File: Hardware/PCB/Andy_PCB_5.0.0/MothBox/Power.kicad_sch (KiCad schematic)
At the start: 23 parts, among them J1 Screw_Terminal_01x02, J2 TYPE-C-31-M-17, Q1 IRF9540N, Q2 TJ10S04M3L,LXHQ, Q3 BC817, U1 XL4015, U2 9V-36V to 12V 5A 60W

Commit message: Andy Added Bolts an consolidated projects
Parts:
- added TPname: TestPoint, TestPoint:TestPoint_THTPad_1.0x1.0mm_Drill0.5mm, symbol Connector:TestPoint
- added U7: ~, symbol attractor:camera2
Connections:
- net at E1.1 (K), F1.1, Q1.3 (S): now also TPname.1
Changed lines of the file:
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@@
+	)
+	(symbol
+		(lib_id "attractor:camera2")
+		(at 110.49 68.58 0)
+		(unit 1)
+		(exclude_from_sim no)
+		(in_bom yes)
+		(on_board yes)
+		(dnp no)
+		(fields_autoplaced yes)
+		(property "Reference" "U7"
+			(at 121.92 67.9449 0)
+			(effects
+				(font
+					(size 1.27 1.27)
+				)
+				(justify left)
+			)
+		)
+		(property "Value" "~"
+			(at 121.92 69.85 0)
+			(effects
+				(font
+					(size 1.27 1.27)
+				)
+				(justify left)
+			)
+		)
+		(property "Footprint" ""
+			(at 110.49 68.58 0)
+			(effects
+				(font
+					(size 1.27 1.27)
+				)
+				(hide yes)
+			)
+		)
+		(property "Datasheet" ""
+			(at 110.49 68.58 0)
+			(effects
+				(font
+					(size 1.27 1.27)
+				)
+				(hide yes)
+			)
+		)
+		(property "Description" ""
+			(at 110.49 68.58 0)
+			(effects
+				(font
+					(size 1.27 1.27)
+				)
+				(hide yes)
+			)
+		)
+		(instances
+			(project ""
+				(path "/9021e528-fc76-4423-a3f3-30f5652071cc/4a573100-9946-48c2-8ae5-35f893607623"
+					(reference "U7")
+					(unit 1)
+				)
+			)
+		)
+	)
+	(symbol
+		(lib_id "Connector:TestPoint")
+		(at 91.44 41.91 0)
+		(unit 1)
+		(exclude_from_sim no)
+		(in_bom yes)
+		(on_board yes)
+		(dnp no)
+		(property "Reference" "TPname"
+			(at 92.964 39.624 0)
+			(effects
+				(font
+					(size 1.27 1.27)
+				)
+				(justify left)
+			)
+		)
+		(property "Value" "TestPoint"
+			(at 93.98 39.8779 0)
+			(effects
+				(font
+					(size 1.27 1.27)
+				)
+				(justify left)
+				(hide yes)
+			)
+		)
+		(property "Footprint" "TestPoint:TestPoint_THTPad_1.0x1.0mm_Drill0.5mm"
+			(at 96.52 41.91 0)
+			(effects
+				(font
+					(size 1.27 1.27)
+				)
+				(hide yes)
+			)
+		)
+		(property "Datasheet" "~"
+			(at 96.52 41.91 0)
+			(effects
+				(font
+					(size 1.27 1.27)
+				)
+				(hide yes)
+			)
+		)
+		(property "Description" "test point"
+			(at 91.44 41.91 0)
+			(effects
+				(font
+					(size 1.27 1.27)
+				)
+				(hide yes)
+			)
+		)
+		(pin "1"
+		)
+		(instances
+			(project ""
+				(path "/9021e528-fc76-4423-a3f3-30f5652071cc/4a573100-9946-48c2-8ae5-35f893607623"
+					(reference "TPname")
+					(unit 1)
+				)
+			)
+		)
 	)
 	(symbol
@@
 			)
 		)
-		(property "Description" "Glass Tube Fuse 7A Plugin,D5xL20mm Disposable fuses ROHS"
+		(property "Description" "Fuse"
 			(at 105.41 41.91 0)
 			(effects

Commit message: made better camera
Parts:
- removed U7: ~, symbol attractor:camera2
- F1: value 7A Fuse -> Polyfuse; footprint Fuse:Fuseholder_Clip-5x20mm_Eaton_1A5601-01_Inline_P20.80x6.76mm_D1.70mm_Horizontal -> Fuse:Fuse_Bourns_MF-RG1000; symbol Device:Fuse -> Device:Polyfuse; LCSC Part no  C5381734 -> (none)
- renumbered E2 to E1, E1 to E2, E4 to E3, E3 to E4, Q3 to Q2, Q2 to Q3, R3 to R1, R1 to R3, TPname to TPname1, U2 to U1, U1 to U3

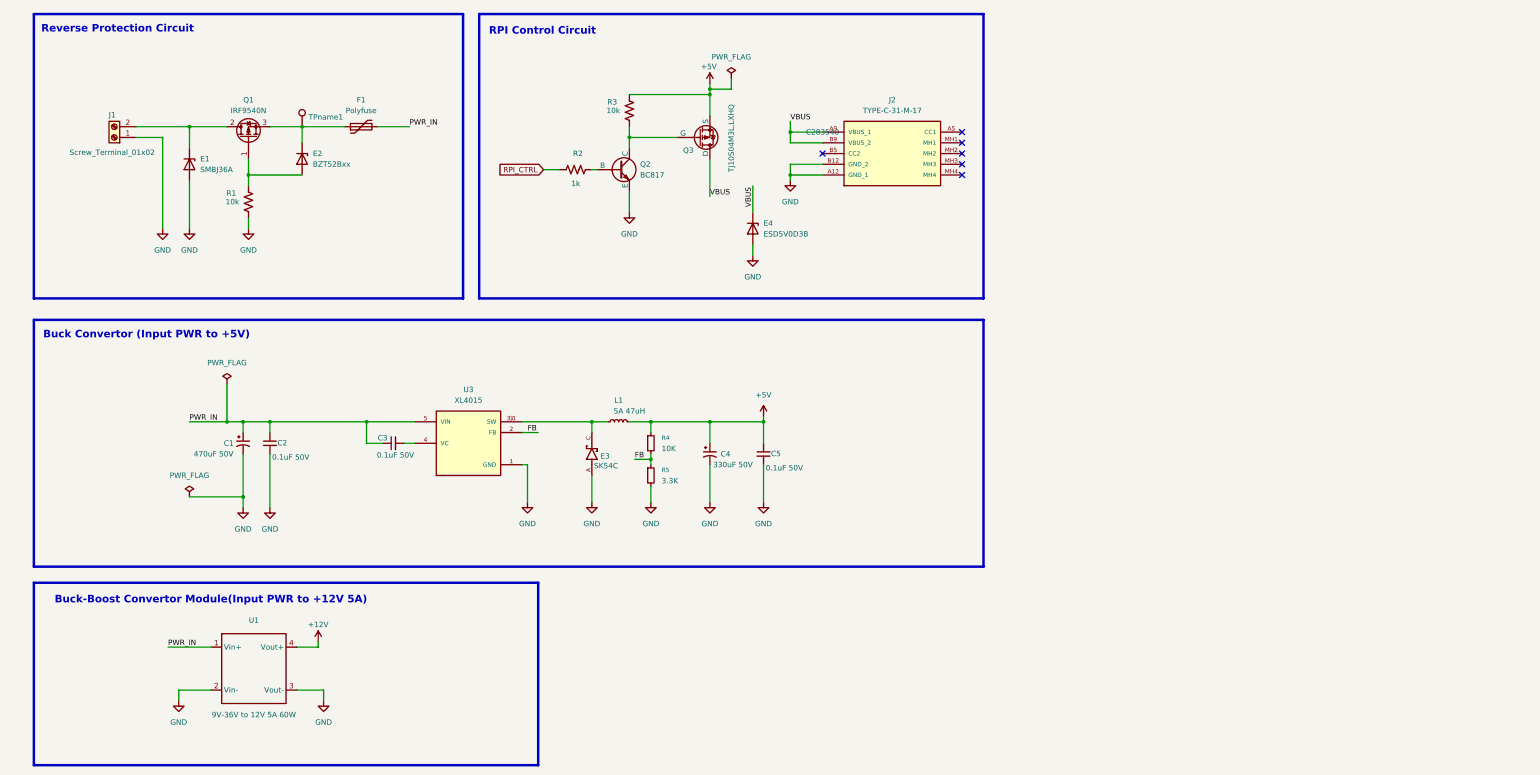
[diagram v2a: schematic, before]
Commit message: added female inverted header
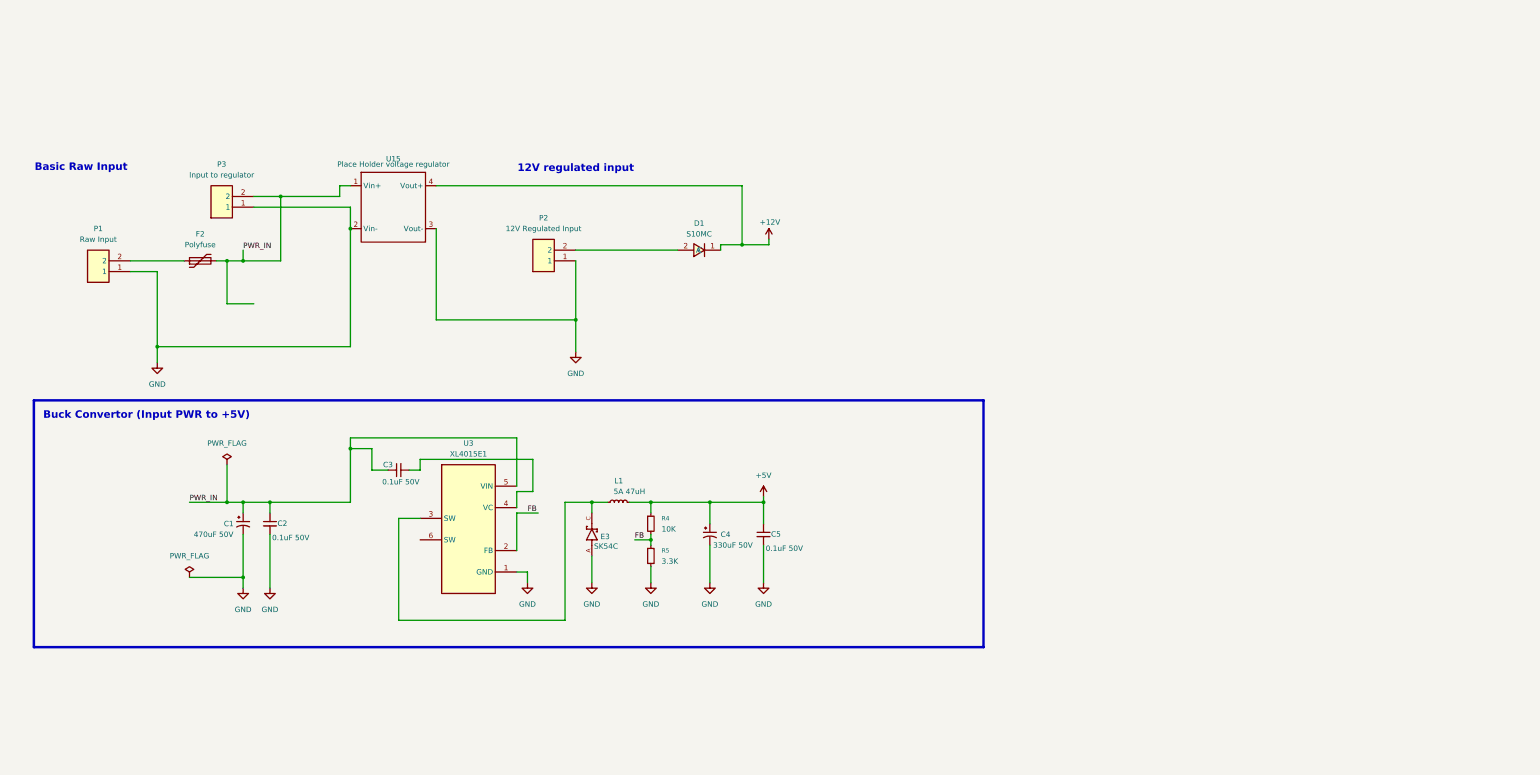
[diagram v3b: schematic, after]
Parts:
- removed E1: SMBJ36A, Diode_SMD:D_SMB, symbol Diode:ESD5Zxx
- removed E2: BZT52Bxx, Diode_SMD:D_SOD-123F, symbol Diode:BZT52Bxx
- removed E4: ESD5V0D3B, Diode_SMD:D_SOD-323, symbol Diode:ESD5Zxx
- removed F1: Polyfuse, Fuse:Fuse_Bourns_MF-RG1000, symbol Device:Polyfuse
- removed J1: Screw_Terminal_01x02, TerminalBlock_RND:TerminalBlock_RND_205-00023_1x02_P10.00mm_Horizontal, symbol Connector:Screw_Terminal_01x02
- removed J2: TYPE-C-31-M-17, TYPE-C-31-M-17:TYPEC31M17, symbol TYPE-C-31-M-17:TYPE-C-31-M-17
- removed Q1: IRF9540N, Package_TO_SOT_THT:TO-220-3_Vertical, symbol Transistor_FET:IRF9540N
- removed Q2: BC817, Package_TO_SOT_SMD:SOT-23, symbol BC817:BC817_NPN_BJT
- removed Q3: TJ10S04M3L,LXHQ, Package_TO_SOT_SMD:TO-252-2, symbol Simulation_SPICE:PMOS
- removed R1, R3: 10k, Resistor_SMD:R_0805_2012Metric, symbol Device:R_US
- removed R2: 1k, Resistor_SMD:R_0805_2012Metric, symbol Device:R_US
- removed TPname1: TestPoint, TestPoint:TestPoint_THTPad_1.0x1.0mm_Drill0.5mm, symbol Connector:TestPoint
- removed U1: 9V-36V to 12V 5A 60W, TerminalBlock:TerminalBlock_MaiXu_MX126-5.0-04P_1x04_P5.00mm, symbol New_Library:Buck-Boost
- added D1: S10MC, easyeda2kicad:SMC_L7.1-W6.2-LS8.1-RD, symbol easyeda2kicad:S10MC
- added F2: Polyfuse, Fuse:Fuse_Bourns_MF-RG1000, symbol Device:Polyfuse
- added P1: Raw Input, easyeda2kicad:CONN-TH_2P-P5.00_WJ500V-5.08-2P, symbol easyeda2kicad:WJ500V-5.08-2P-14-00A
- added P2: 12V Regulated Input, easyeda2kicad:CONN-TH_2P-P5.00_WJ500V-5.08-2P, symbol easyeda2kicad:WJ500V-5.08-2P-14-00A
- added P3: Input to regulator, easyeda2kicad:CONN-TH_2P-P5.00_WJ500V-5.08-2P, symbol easyeda2kicad:WJ500V-5.08-2P-14-00A
- added U15: Place Holder voltage regulator, symbol New_Library:Buck-Boost
- U3: value XL4015 -> XL4015E1; footprint XL4015:CONV_XL4015 -> easyeda2kicad:TO-263-5_L10.2-W8.9-P1.70-TL; symbol XL4015:XL4015 -> easyeda2kicad:XL4015E1; LCSC Part (none) -> C51661
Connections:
- net +12V: now also D1.1 (C), U15.4 (Vout+)
- net GND: now also P1.1, P2.1, P3.1, U15.2 (Vin-), U15.3 (Vout-)
- net PWR_IN: now also F2.2, P3.2, U15.1 (Vin+)
- net at E3.C, L1.1, U3.3 (SW): no longer U3.3.1 (SW)
- new net: D1.2 (A), P2.2
- new net: F2.1, P1.2
- no-connect marks 6 -> 0
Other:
- note added: "12V regulated input"
- note added: "Basic Raw Input"
- note removed: "Buck-Boost Convertor Module(Input PWR to +12V 5A)"
- note removed: "RPI Control Circuit"
- note removed: "Reverse Protection Circuit"
- moved on the sheet: C1, C2, C3, C4, C5, E3, L1, R4, R5

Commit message: arranged stuff better
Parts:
- added Q1: BC817, Package_TO_SOT_SMD:SOT-23, symbol BC817:BC817_NPN_BJT
- added Q2: TJ10S04M3L,LXHQ, Package_TO_SOT_SMD:TO-252-2, symbol Simulation_SPICE:PMOS
- added R1: 10k, Resistor_SMD:R_0805_2012Metric, symbol Device:R_US
- F2: footprint Fuse:Fuse_Bourns_MF-RG1000 -> easyeda2kicad:F0805; symbol Device:Polyfuse -> easyeda2kicad:0805L010_60WR; LCSC Part (none) -> C22435897
- P1, P2, P3: footprint easyeda2kicad:CONN-TH_2P-P5.00_WJ500V-5.08-2P -> easyeda2kicad:CONN-TH_DB301V-3.5-2P-GN; symbol easyeda2kicad:WJ500V-5.08-2P-14-00A -> easyeda2kicad:DB301V-3.5-2P-GN; LCSC Part C8465 -> C695629
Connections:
- net GND: now also Q1.2 (E)
- net PWR_IN: now also F2.1, Q2.3 (S), R1.2; no longer F2.2, U15.1 (Vin+)
- net at P1.2: now also F2.2; no longer F2.1
- new net: Q1.3 (C), Q2.2 (G), R1.1
- new net: Q2.1 (D), U15.1 (Vin+)
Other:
- note added: "Switch the Regulator on and Off"

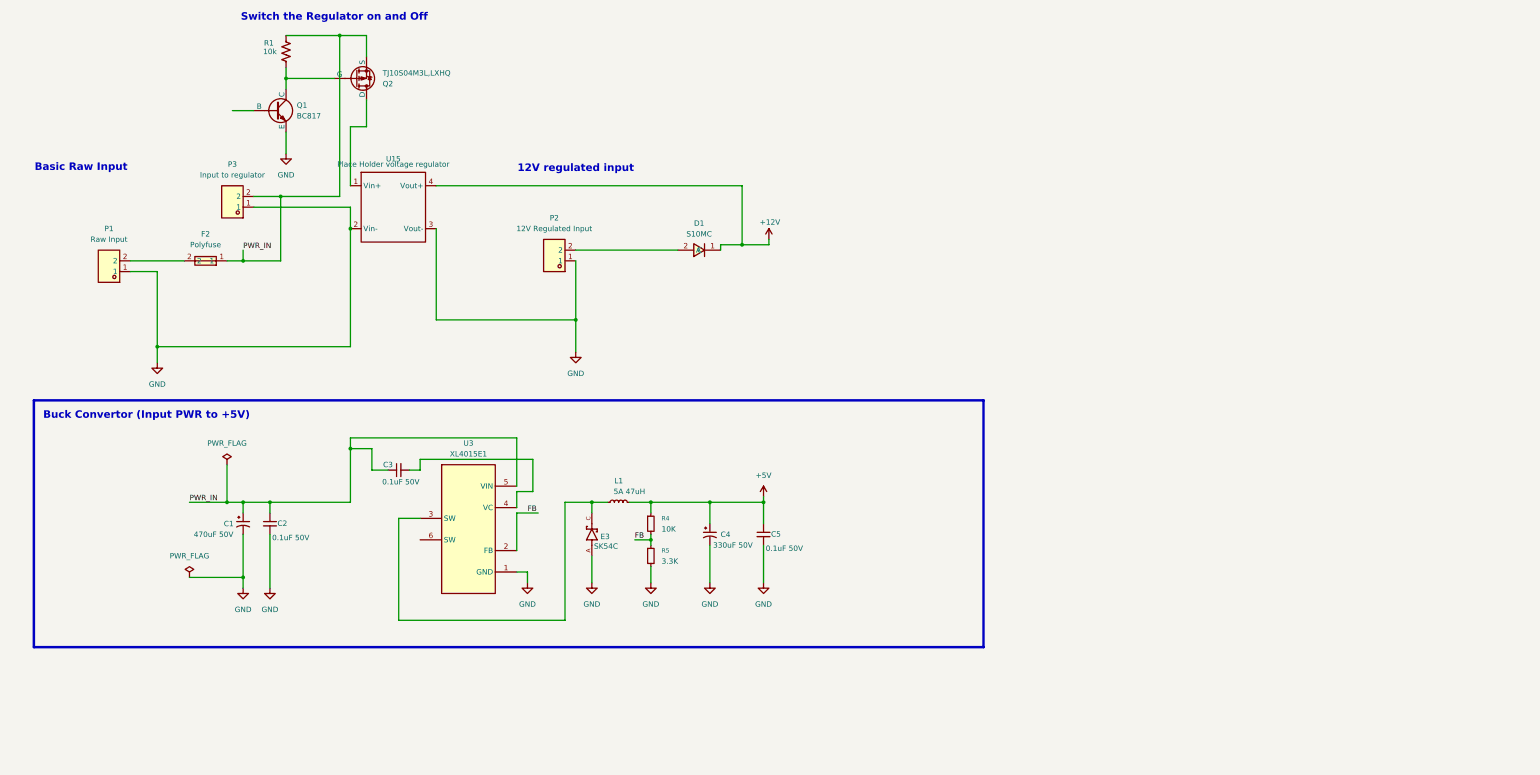
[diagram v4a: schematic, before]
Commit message: Added adafruit current sensor
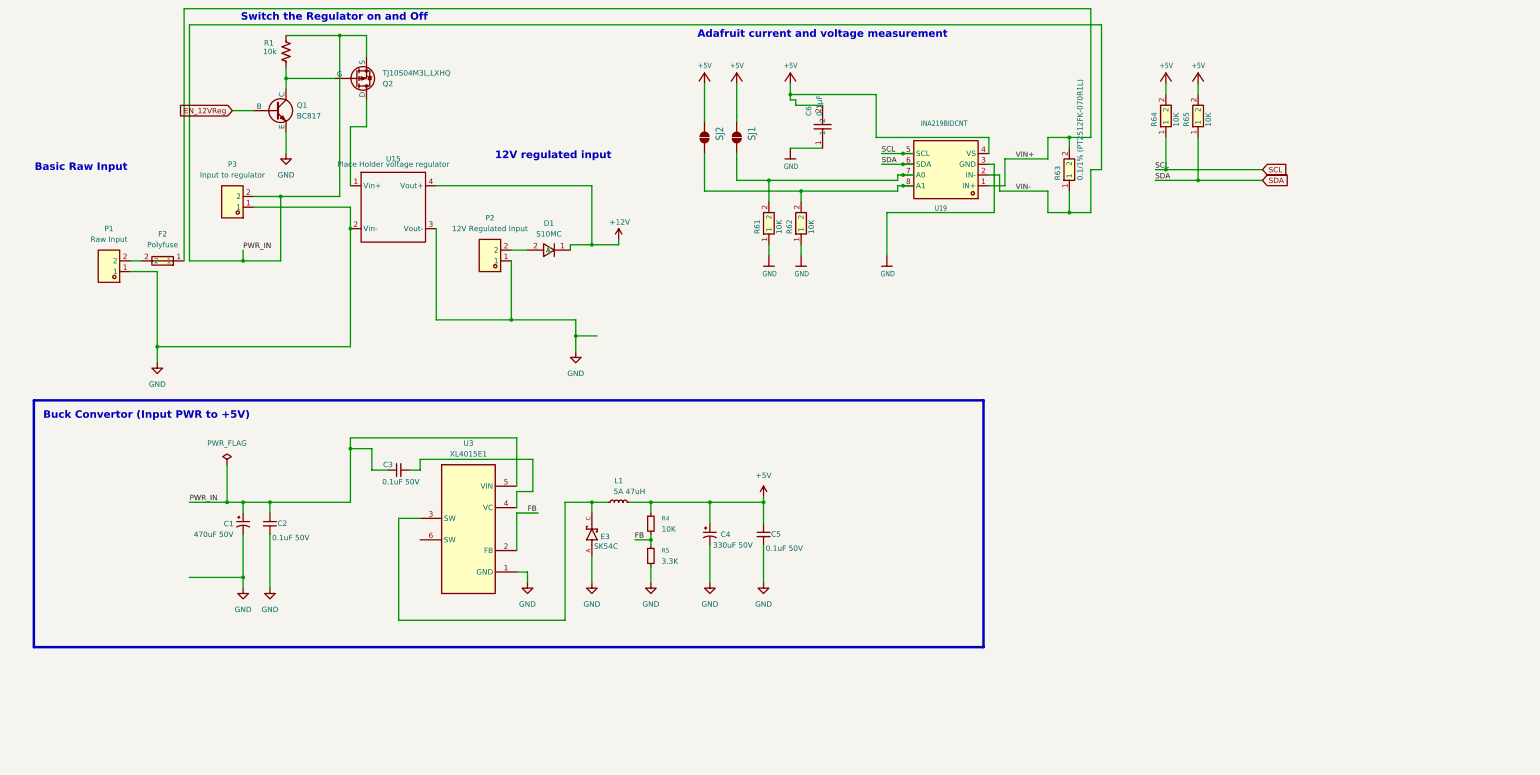
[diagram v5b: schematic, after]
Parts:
- added C6: 0.1µF, easyeda2kicad:C0603, symbol easyeda2kicad:CC0603KRX7R9BB104
- added R61, R62, R64, R65: 10K, easyeda2kicad:R0603, symbol easyeda2kicad:FRC0603J103TS
- added R63: 0.1/1% (PT2512FK-070R1L), easyeda2kicad:R2512, symbol easyeda2kicad:PCSR2512BR100M6
- added SJ1: SOLDERJUMPERREFLOW_NOPASTE, Jumper:SolderJumper-2_P1.3mm_Open_RoundedPad1.0x1.5mm, symbol Jumper:SolderJumper_2_Open
- added SJ2: SOLDERJUMPERREFLOW_NOPASTE, Jumper:SolderJumper-2_P1.3mm_Open_TrianglePad1.0x1.5mm, symbol Jumper:SolderJumper_2_Open
- added U19: INA219BIDCNT, easyeda2kicad:SOT-23-8_L3.0-W1.7-P0.65-LS2.8-BR, symbol easyeda2kicad:INA219AIDCNR
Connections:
- net +5V: now also C6.2, R64.2, R65.2, SJ1.1 (A), SJ2.1 (A), U19.4 (VS)
- net GND: now also C6.1, R61.1, R62.1, U19.3 (GND)
- net PWR_IN: now also R63.1, U19.2 (IN-); no longer F2.1
- net EN_12VReg: now reaches Q1.1 (B)
- new net: R62.2, SJ2.2 (B), U19.8 (A1)
- new net: R61.2, SJ1.2 (B), U19.7 (A0)
- new net SCL: R64.1, U19.5 (SCL)
- new net SDA: R65.1, U19.6 (SDA)
- new net VIN+: F2.1, R63.2, U19.1 (IN+)
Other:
- note added: "Adafruit current and voltage measurement"
- moved on the sheet: D1, F2, P2
